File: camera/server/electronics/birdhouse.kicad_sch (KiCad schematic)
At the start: 17 parts, among them Q1 PN2222A, Q2 2N6292

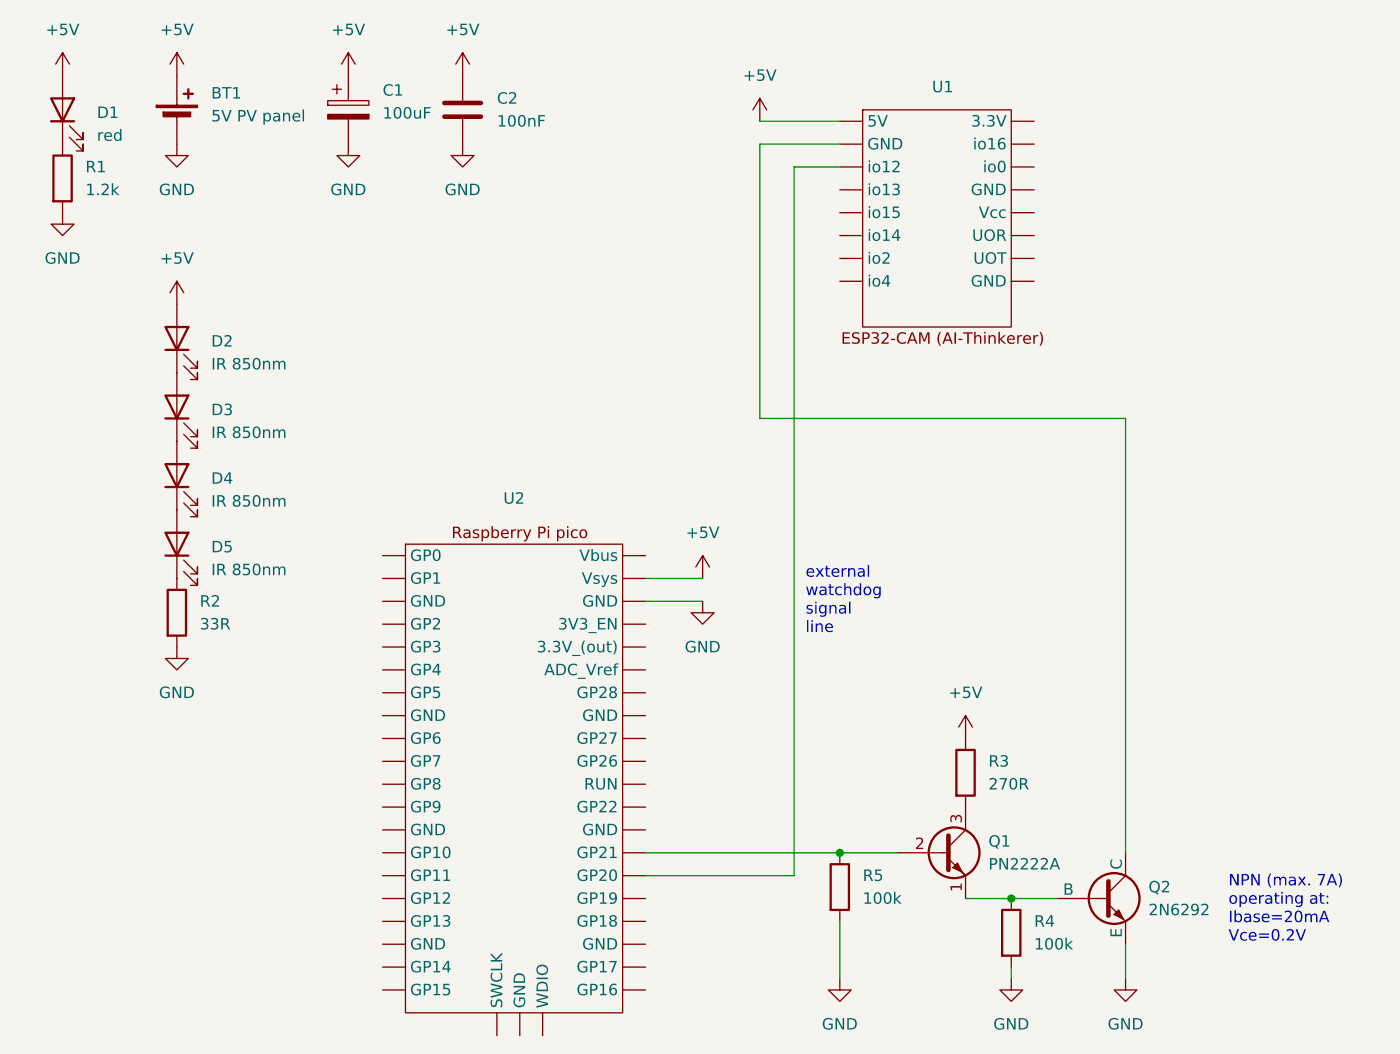
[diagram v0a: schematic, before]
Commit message: added notes on IR LEDs and fixed capacitor value
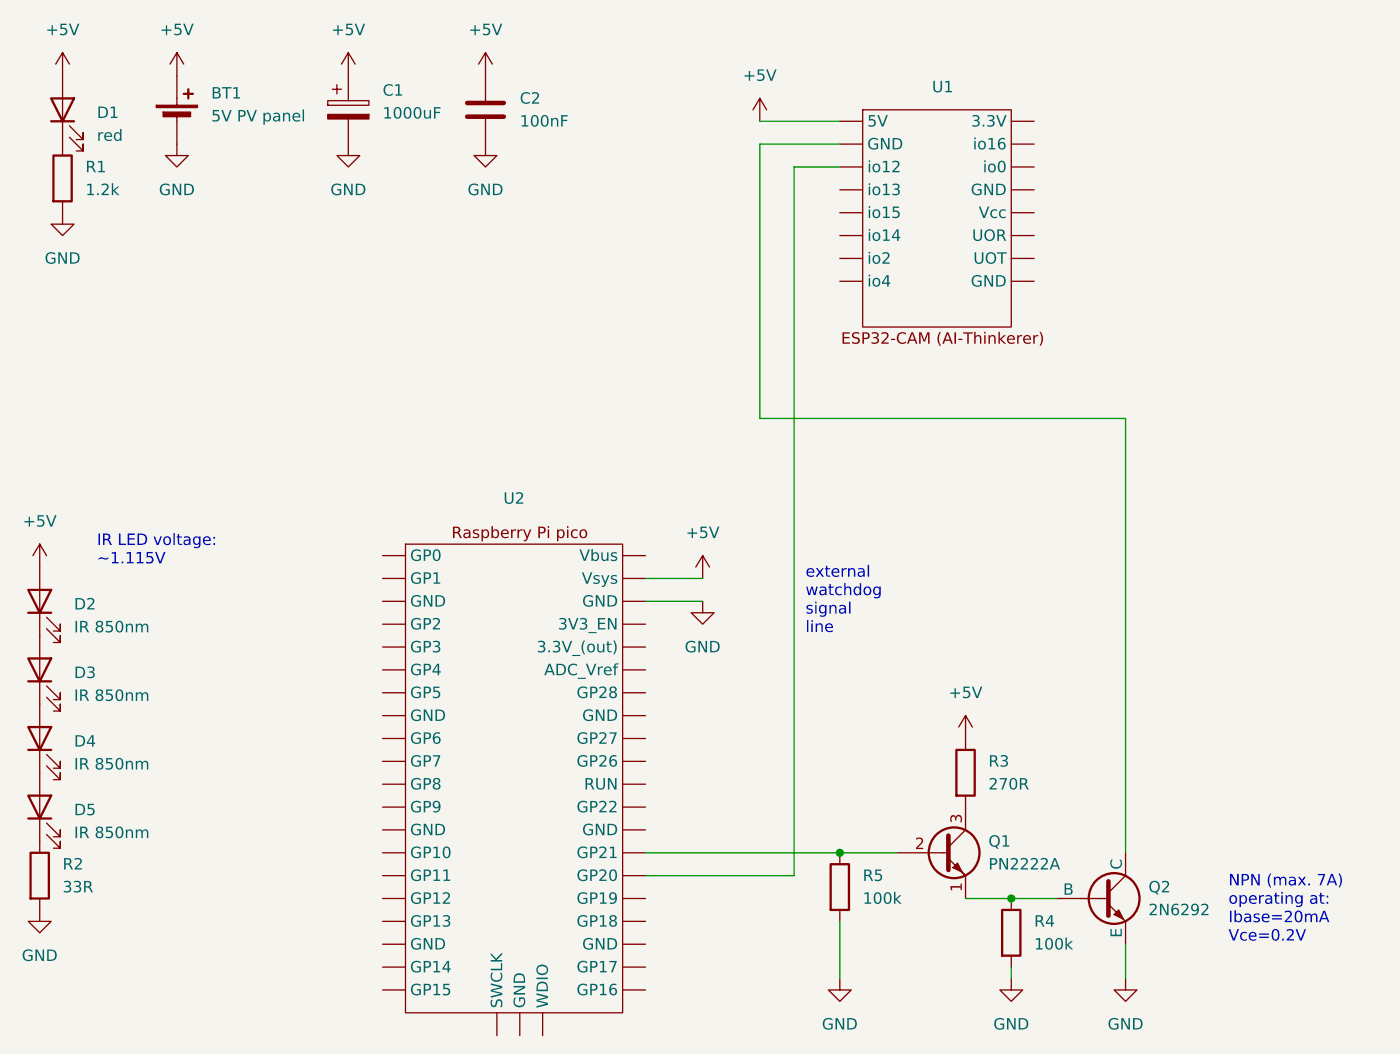
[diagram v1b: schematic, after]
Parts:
- C1: value 100uF -> 1000uF
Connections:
- new net: U1. (io4), U2. (WDIO)
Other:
- note added: "IR LED voltage: ~1.115V"
- moved on the sheet: C2, D2, D3, D4, D5, R2
